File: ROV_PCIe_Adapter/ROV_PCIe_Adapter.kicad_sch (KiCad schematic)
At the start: 13 parts, among them J1 525591652, J2 691311500102, Q1 AO3401A

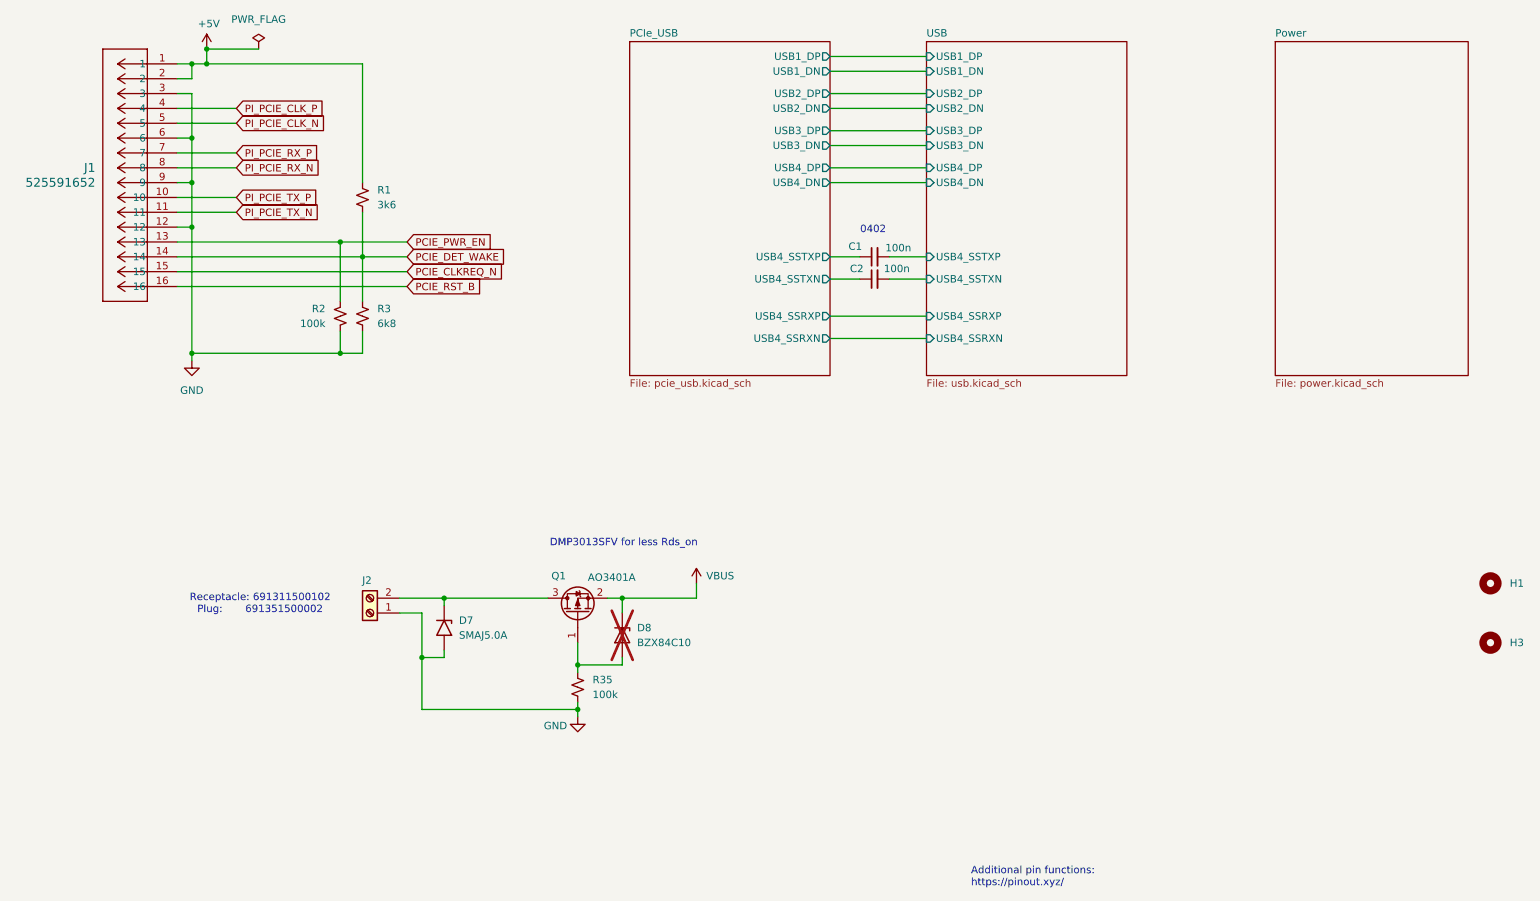
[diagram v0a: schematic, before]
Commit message: updates (fe1.1s board deprecated)
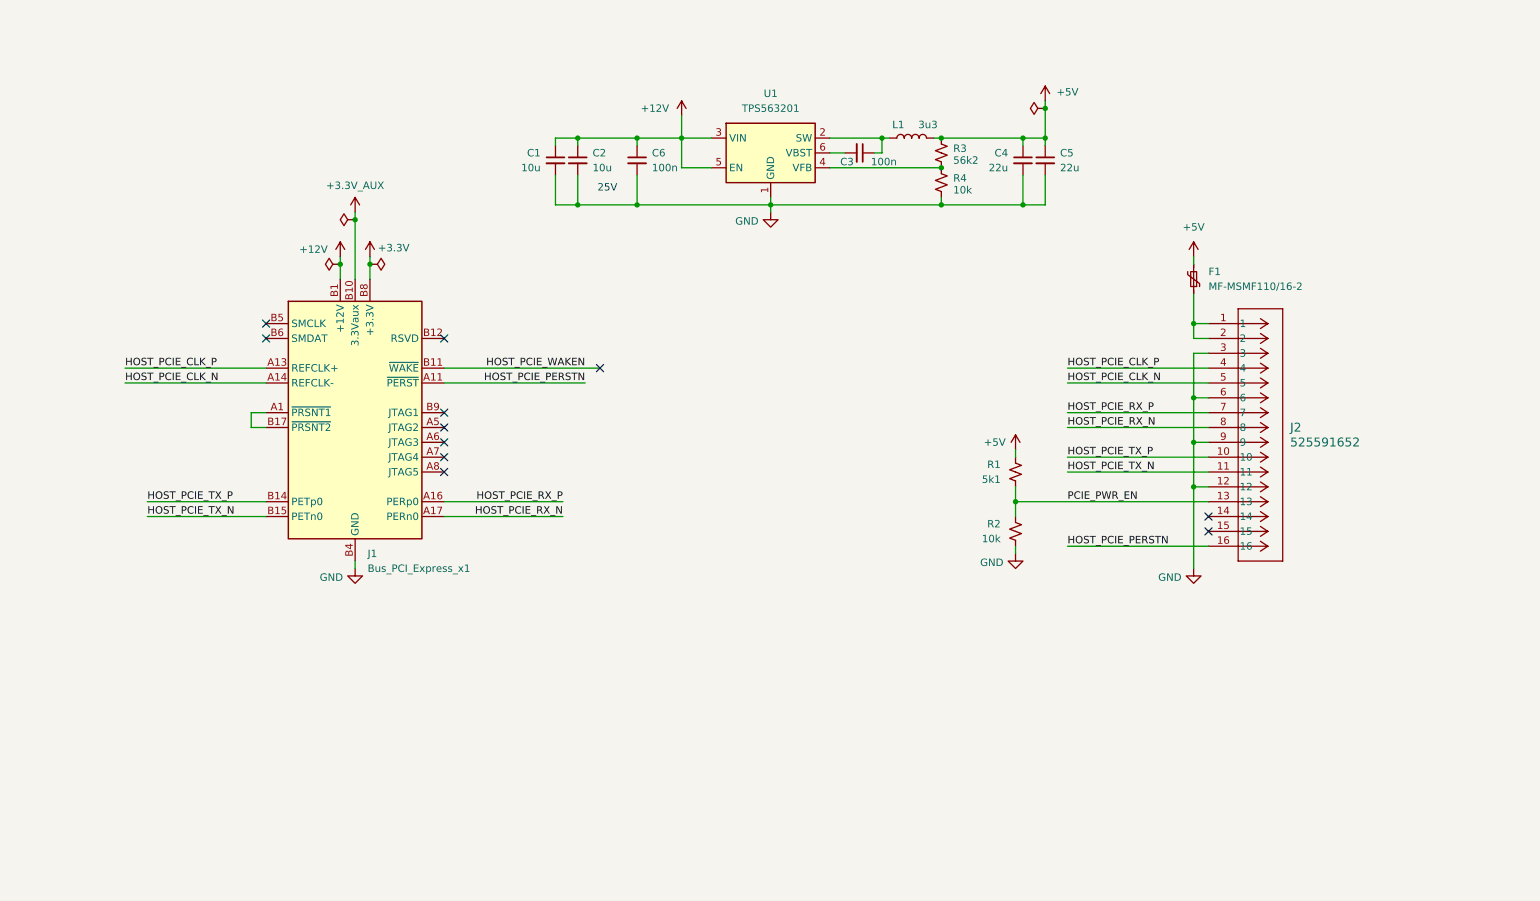
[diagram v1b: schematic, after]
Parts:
- removed D7: SMAJ5.0A, Diode_SMD:D_SMA, symbol Diode:SMAJ5.0A
- removed D8: BZX84C10, Diode_SMD:D_0402_1005Metric, symbol Device:D_Zener
- removed H1, H3: MountingHole, MountingHole:MountingHole_3.2mm_M3, symbol Mechanical:MountingHole
- removed J1: 525591652, snadol:525591652, symbol snadol:525591652
- removed J2: 691311500102, Connector_THT_Wurth:J_Wurth_WR-TBL_691311500102, symbol Connector:Screw_Terminal_01x02
- removed Q1: AO3401A, Package_TO_SOT_SMD:SOT-23, symbol Transistor_FET:AO3401A
- removed R35: 100k, Resistor_SMD:R_0603_1608Metric, symbol Device:R_Small_US
- added C3, C6: 100n, Capacitor_SMD:C_0402_1005Metric, symbol Device:C_Small
- added C4, C5: 22u, Capacitor_SMD:C_0805_2012Metric, symbol Device:C_Small
- added F1: MF-MSMF110/16-2, Fuse:Fuse_1812_4532Metric, symbol Device:Polyfuse_Small
- added J1: Bus_PCI_Express_x1, Connector_PCBEdge:BUS_PCIexpress_x1, symbol Connector:Bus_PCI_Express_x1
- added J2: 525591652, snadol:525591652, symbol snadol:525591652
- added L1: 3u3, Inductor_SMD:L_Taiyo-Yuden_MD-5050, symbol Device:L
- added R4: 10k, Resistor_SMD:R_0603_1608Metric, symbol Device:R_Small_US
- added U1: TPS563201, Package_TO_SOT_SMD:SOT-23-6, symbol Regulator_Switching:TPS563201
- C1, C2: value 100n -> 10u; footprint Capacitor_SMD:C_0402_1005Metric -> Capacitor_SMD:C_0805_2012Metric; Part Number CL05B104KO5NNNC -> (none)
- R1: value 3k6 -> 5k1; Part Number RC0603FR-073K6L -> (none)
- R2: value 100k -> 10k; Part Number RC0603FR-07100KL -> (none)
- R3: value 6k8 -> 56k2; Part Number RC0603FR-076K8L -> (none)
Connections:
- net PCIe_USB/USB4_SSTXP is gone; now on net +12V: C1.1
- net USB/USB4_SSTXN is gone; now on net GND: C2.2
- net USB/USB4_SSTXP is gone; now on net GND: C1.2
- net +5V: now also R3.1, C4.1, C5.1, F1.2, L1.2
- net GND: now also C4.2, C5.2, C6.2, J1.A12 (GND), J1.A15 (GND), J1.A18 (GND), J1.A4 (GND), J1.B13 (GND), J1.B16 (GND), J1.B18 (GND), J1.B4 (GND), J1.B7 (GND), J2.12, J2.3, J2.6, J2.9, R4.2, U1.1 (GND); no longer R3.2
- net PCIE_PWR_EN: now also R1.2, J2.13
- removed net PCIE_DET_WAKE: R1.2, R3.1
- net PCIe_USB/USB4_SSTXN renamed +12V
- net +12V: now also C6.1, J1.A2 (+12V), J1.A3 (+12V), J1.B1 (+12V), J1.B2 (+12V), J1.B3 (+12V), U1.3 (VIN), U1.5 (EN)
- new net: C3.1, L1.1, U1.2 (SW)
- new net: C3.2, U1.6 (VBST)
- new net: F1.1, J2.1, J2.2
- new net: R3.2, R4.1, U1.4 (VFB)
- new net: J1.A1 (~{PRSNT1}), J1.B17 (~{PRSNT2})
- new net +3.3V: J1.A10 (+3.3V), J1.A9 (+3.3V), J1.B8 (+3.3V)
- new net +3.3V_AUX: J1.B10 (3.3Vaux)
- new net HOST_PCIE_CLK_N: J1.A14 (REFCLK-), J2.5
- new net HOST_PCIE_CLK_P: J1.A13 (REFCLK+), J2.4
- new net HOST_PCIE_PERSTN: J1.A11 (~{PERST}), J2.16
- new net HOST_PCIE_RX_N: J1.A17 (PERn0), J2.8
- new net HOST_PCIE_RX_P: J1.A16 (PERp0), J2.7
- new net HOST_PCIE_TX_N: J1.B15 (PETn0), J2.11
- new net HOST_PCIE_TX_P: J1.B14 (PETp0), J2.10
- new net HOST_PCIE_WAKEN: J1.B11 (~{WAKE})
- no-connect marks 0 -> 11
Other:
- removed sheet PCIe_USB
- removed sheet Power
- removed sheet USB
- note added: "25V"
- note removed: "0402"
- note removed: "Additional pin functions: https://pinout.xyz/"
- note removed: "DMP3013SFV for less Rds_on"
- note removed: "Receptacle: 691311500102 Plug: 691351500002"

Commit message: changes
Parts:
- added C10, C8: 100n, Capacitor_SMD:C_0402_1005Metric, symbol Device:C_Small
- added C7, C9: 22u, Capacitor_SMD:C_0805_2012Metric, symbol Device:C_Small
- C1, C2, C6: Voltage Rating (none) -> 25
- C3, C4, C5: Voltage Rating (none) -> 10
- F1: value MF-MSMF110/16-2 -> MF-MSMF150/12-2
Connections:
- net +12V: now also C7.1, C8.1
- net GND: now also C10.2, C7.2, C8.2, C9.2
- net at F1.1, J2.1, J2.2: now also C10.1, C9.1
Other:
- moved on the sheet: F1

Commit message: changes
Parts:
- added R5: 0R, Resistor_SMD:R_0402_1005Metric, symbol Device:R_Small_US
- C1, C2: Part Number (none) -> CL21A106KAYNNNE
- C10, C3: Part Number (none) -> CL05B104KA5NNNC; Voltage Rating 10 -> 25
- C4, C9: Part Number (none) -> CL21A226MAQNNNE; Voltage Rating 10 -> 25
- C5: value 22u -> 10p; footprint Capacitor_SMD:C_0805_2012Metric -> Capacitor_SMD:C_0402_1005Metric; Part Number (none) -> CL05A104KA5NNNC; Voltage Rating 10 -> (none); now not fitted
- C6, C8: Part Number (none) -> CL05B104KA5NNNC
- C7: value 22u -> 10u; Part Number (none) -> CL21A106KAYNNNE
- F1: value MF-MSMF150/12-2 -> MF-MSMF150/12X-2; Part Number (none) -> MF-MSMF150/12X-2
- J1: now left out of the parts list
- J2: Part Number (none) -> 525591652
- L1: Part Number (none) -> BWVC005050403R3M00
- R1: Part Number (none) -> RC0603FR-075K1L
- R2, R4: Part Number (none) -> RC0603FR-0710KL
- R3: Part Number (none) -> RC0603FR-0756K2L
- U1: Part Number (none) -> TPS563201DDCR
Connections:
- net GND: no longer C5.2
- net at U1.6 (VBST): now also R5.1; no longer C3.2
- net at R3.2, R4.1, U1.4 (VFB): now also C5.2
- new net: C3.2, R5.2
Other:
- moved on the sheet: C4

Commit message: final
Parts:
- added D1, D2: LED, LED_SMD:LED_0603_1608Metric, symbol Device:LED
- added R6: 5k1, Resistor_SMD:R_0603_1608Metric, symbol Device:R_Small_US
- added R7: 1k6, Resistor_SMD:R_0603_1608Metric, symbol Device:R_Small_US
- C1, C2, C7: Part Number CL21A106KAYNNNE -> CC0805KRX5R8BB106
- C10, C3, C6, C8: Part Number CL05B104KA5NNNC -> CC0402KRX7R8BB104
- C4, C9: footprint Capacitor_SMD:C_0805_2012Metric -> Capacitor_SMD:C_1206_3216Metric; Part Number CL21A226MAQNNNE -> CC1206KKX5R8BB226
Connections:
- net +12V: now also D1.2 (A)
- net +5V: now also D2.2 (A)
- net GND: now also R6.2, R7.2
- new net: D1.1 (K), R6.1
- new net: D2.1 (K), R7.1
